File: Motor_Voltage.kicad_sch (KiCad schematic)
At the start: 15 parts

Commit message: mini review notes
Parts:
- gave numbers to parts that had none: 15
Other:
- note added: "V+ and V- not descriptive bruh"
- note added: "V_IN_2 change to output"
- note added: "V_IN_2 to V_IN_MOT to be more descriptive"
- note added: "change HVGND and LVGND global labels into just a hierarchal pin"
- note added: "hierarchal pin works like label"
- note added: "line with line tool and "e""

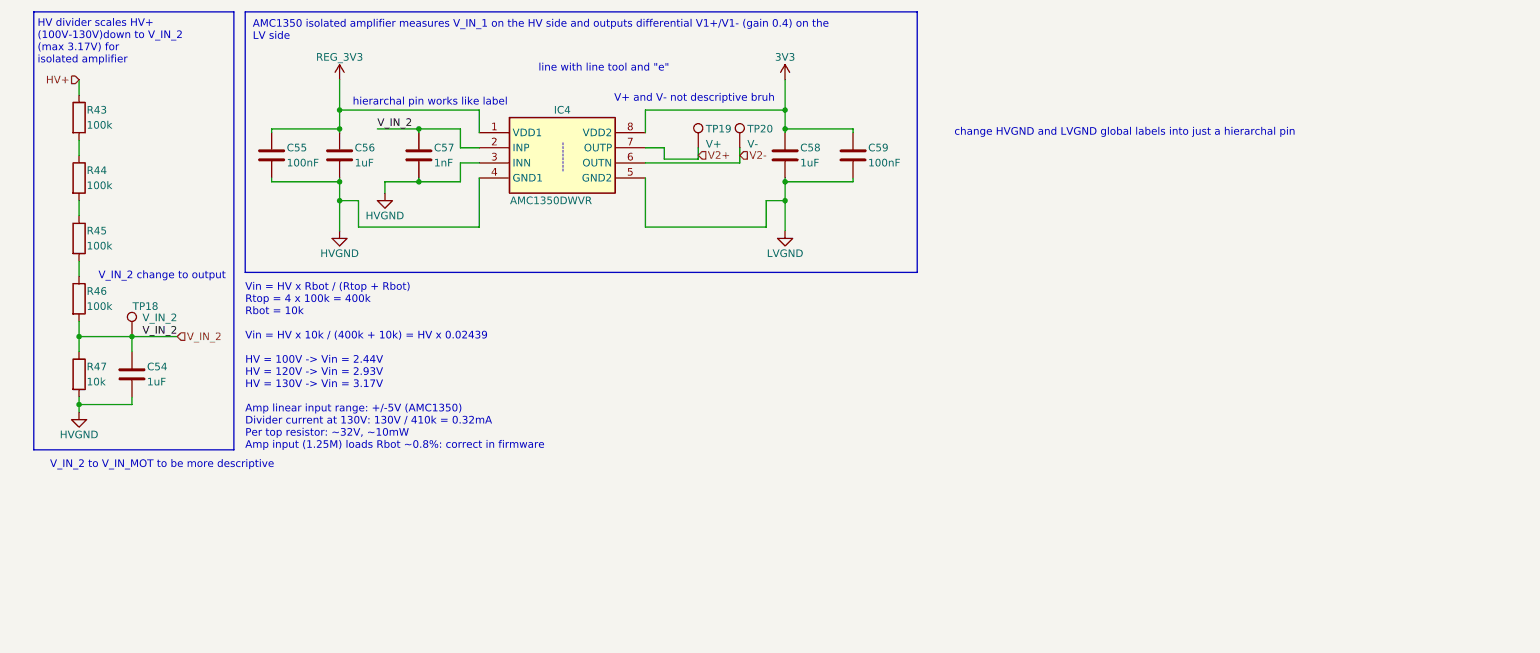
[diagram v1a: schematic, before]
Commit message: fixed battery voltage & motor voltage
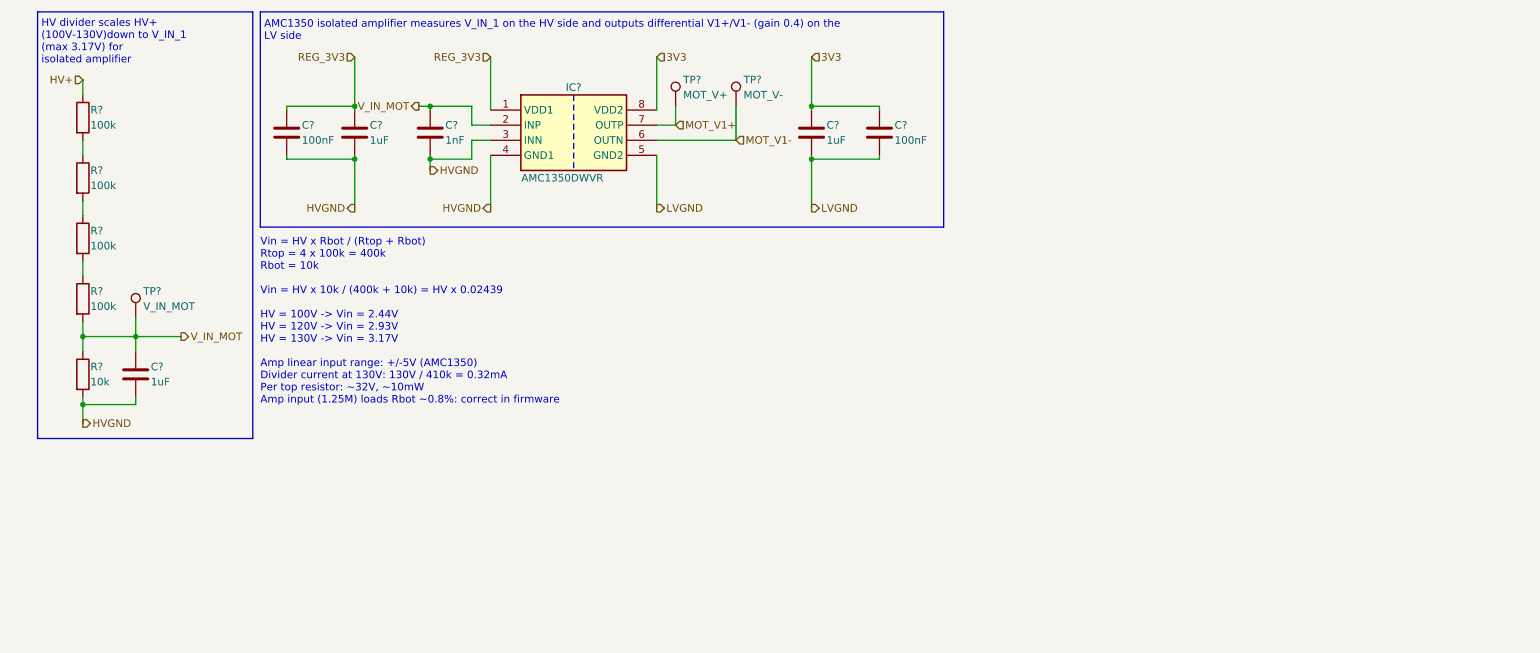
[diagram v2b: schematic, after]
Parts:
- removed C54, C56, C58: 1uF, symbol Device:C
- removed C55, C59: 100nF, symbol Device:C
- removed C57: 1nF, symbol Device:C
- removed IC4: AMC1350DWVR, ActivePrecharge-RevB:SOIC127P1150X280-8N, symbol AMC1350:AMC1350DWVR
- removed R43, R44, R45, R46: 100k, Package_DIP:DIP-8_W7.62mm, symbol Device:R
- removed R47: 10k, Package_DIP:DIP-8_W7.62mm, symbol Device:R
- removed TP18: V_IN_2, symbol Connector:TestPoint
- removed TP19: V+, symbol Connector:TestPoint
- removed TP20: V-, symbol Connector:TestPoint
- added C? (x3): 1uF, symbol Device:C
- added C?: 1nF, symbol Device:C
- added C? (x2): 100nF, symbol Device:C
- added IC?: AMC1350DWVR, ActivePrecharge-RevB:SOIC127P1150X280-8N, symbol AMC1350:AMC1350DWVR
- added R?: 10k, Package_DIP:DIP-8_W7.62mm, symbol Device:R
- added R? (x4): 100k, Package_DIP:DIP-8_W7.62mm, symbol Device:R
- added TP?: V_IN_MOT, TestPoint:TestPoint_Loop_D1.80mm_Drill1.0mm_Beaded, symbol lhrs_misc:Multimeter_TP
- added TP?: MOT_V-, TestPoint:TestPoint_Loop_D1.80mm_Drill1.0mm_Beaded, symbol lhrs_misc:Multimeter_TP
- added TP?: MOT_V+, TestPoint:TestPoint_Loop_D1.80mm_Drill1.0mm_Beaded, symbol lhrs_misc:Multimeter_TP
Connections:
- net 3V3: now also C?.1, C?.1, IC?.8 (VDD2)
- net HV+: now also R?.1
- net HVGND: now also C?.2, C?.2, C?.2, C?.2, IC?.3 (INN), IC?.4 (GND1), R?.2
- net LVGND: now also C?.2, C?.2, IC?.5 (GND2)
- net REG_3V3: now also C?.1, C?.1, IC?.1 (VDD1)
- new net: R?.1, R?.2 (x3)
- new net MOT_V1+: IC?.7 (OUTP), TP?.1
- new net MOT_V1-: IC?.6 (OUTN), TP?.1
- new net V_IN_MOT: C?.1, C?.1, IC?.2 (INP), R?.1, R?.2, TP?.1
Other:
- note added: "HV divider scales HV+ (100V-130V)down to V_IN_1 (max 3.17V) for isolated amplifier"
- note removed: "--------"
- note removed: "HV divider scales HV+ (100V-130V)down to V_IN_2 (max 3.17V) for isolated amplifier"
- note removed: "V+ and V- not descriptive bruh"
- note removed: "V_IN_2 change to output"
- note removed: "V_IN_2 to V_IN_MOT to be more descriptive"
- note removed: "change HVGND and LVGND global labels into just a hierarchal pin"
- note removed: "hierarchal pin works like label"
- note removed: "line with line tool and "e""

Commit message: fixed lv
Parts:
- gave numbers to parts that had none: 15
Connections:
- net MOT_V1+ renamed MOT_V+
- net MOT_V1- renamed MOT_V-
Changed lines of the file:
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@@
 		)
 	)
-	(hierarchical_label "MOT_V1-"
+	(hierarchical_label "MOT_V-"
 		(shape input)
 		(at 132.08 35.56 0)
@@
 		)
 	)
-	(hierarchical_label "MOT_V1+"
+	(hierarchical_label "MOT_V+"
 		(shape input)
 		(at 121.92 33.02 0)
@@
 		(in_pos_files yes)
 		(dnp no)
-		(property "Reference" "TP?"
+		(property "Reference" "TP18"
 			(at 32.385 60.96 0)
 			(show_name no)
@@
 			(project "PS-PrechargeBoard"
 				(path "/74d17fe6-68d4-4bd7-954a-e2bbb58b1f1e/ad0f3840-ec25-4ea7-b025-1d3129a06533/c3a8be03-ea6f-409a-9c75-c47de7f52741"
-					(reference "TP?")
+					(reference "TP18")
 					(unit 1)
 				)
@@
 		(in_pos_files yes)
 		(dnp no)
-		(property "Reference" "C?"
+		(property "Reference" "C56"
 			(at 70.485 33.02 0)
 			(show_name no)
@@
 			(project "PS-PrechargeBoard"
 				(path "/74d17fe6-68d4-4bd7-954a-e2bbb58b1f1e/ad0f3840-ec25-4ea7-b025-1d3129a06533/c3a8be03-ea6f-409a-9c75-c47de7f52741"
-					(reference "C?")
+					(reference "C56")
 					(unit 1)
 				)
@@
 		(in_pos_files yes)
 		(dnp no)
-		(property "Reference" "TP?"
+		(property "Reference" "TP20"
 			(at 133.35 25.4 0)
 			(show_name no)
@@
 			(project "PS-PrechargeBoard"
 				(path "/74d17fe6-68d4-4bd7-954a-e2bbb58b1f1e/ad0f3840-ec25-4ea7-b025-1d3129a06533/c3a8be03-ea6f-409a-9c75-c47de7f52741"
-					(reference "TP?")
+					(reference "TP20")
 					(unit 1)
 				)
@@
 		(in_pos_files yes)
 		(dnp no)
-		(property "Reference" "R?"
+		(property "Reference" "R47"
 			(at 23.495 73.66 0)
 			(show_name no)
@@
 			(project "PS-PrechargeBoard"
 				(path "/74d17fe6-68d4-4bd7-954a-e2bbb58b1f1e/ad0f3840-ec25-4ea7-b025-1d3129a06533/c3a8be03-ea6f-409a-9c75-c47de7f52741"
-					(reference "R?")
+					(reference "R47")
 					(unit 1)
 				)
@@
 		(in_pos_files yes)
 		(dnp no)
-		(property "Reference" "C?"
+		(property "Reference" "C57"
 			(at 83.185 33.02 0)
 			(show_name no)
@@
 			(project "PS-PrechargeBoard"
 				(path "/74d17fe6-68d4-4bd7-954a-e2bbb58b1f1e/ad0f3840-ec25-4ea7-b025-1d3129a06533/c3a8be03-ea6f-409a-9c75-c47de7f52741"
-					(reference "C?")
+					(reference "C57")
 					(unit 1)
 				)
@@
 		(in_pos_files yes)
 		(dnp no)
-		(property "Reference" "C?"
+		(property "Reference" "C54"
 			(at 33.655 73.66 0)
 			(show_name no)
@@
 			(project "PS-PrechargeBoard"
 				(path "/74d17fe6-68d4-4bd7-954a-e2bbb58b1f1e/ad0f3840-ec25-4ea7-b025-1d3129a06533/c3a8be03-ea6f-409a-9c75-c47de7f52741"
-					(reference "C?")
+					(reference "C54")
 					(unit 1)
 				)
@@
 		(in_pos_files yes)
 		(dnp no)
-		(property "Reference" "TP?"
+		(property "Reference" "TP19"
 			(at 123.19 25.4 0)
 			(show_name no)
@@
 			(project "PS-PrechargeBoard"
 				(path "/74d17fe6-68d4-4bd7-954a-e2bbb58b1f1e/ad0f3840-ec25-4ea7-b025-1d3129a06533/c3a8be03-ea6f-409a-9c75-c47de7f52741"
-					(reference "TP?")
+					(reference "TP19")
 					(unit 1)
 				)
@@
 		(in_pos_files yes)
 		(dnp no)
-		(property "Reference" "C?"
+		(property "Reference" "C58"
 			(at 147.32 33.02 0)
 			(show_name no)
@@
 			(project "PS-PrechargeBoard"
 				(path "/74d17fe6-68d4-4bd7-954a-e2bbb58b1f1e/ad0f3840-ec25-4ea7-b025-1d3129a06533/c3a8be03-ea6f-409a-9c75-c47de7f52741"
-					(reference "C?")
+					(reference "C58")
 					(unit 1)
 				)
@@
 		(in_pos_files yes)
 		(dnp no)
-		(property "Reference" "IC?"
+		(property "Reference" "IC4"
 			(at 104.775 26.67 0)
 			(show_name no)
@@
 			(project "PS-PrechargeBoard"
 				(path "/74d17fe6-68d4-4bd7-954a-e2bbb58b1f1e/ad0f3840-ec25-4ea7-b025-1d3129a06533/c3a8be03-ea6f-409a-9c75-c47de7f52741"
-					(reference "IC?")
+					(reference "IC4")
 					(unit 1)
 				)
@@
 		(in_pos_files yes)
 		(dnp no)
-		(property "Reference" "C?"
+		(property "Reference" "C59"
 			(at 158.75 33.02 0)
 			(show_name no)
@@
 			(project "PS-PrechargeBoard"
 				(path "/74d17fe6-68d4-4bd7-954a-e2bbb58b1f1e/ad0f3840-ec25-4ea7-b025-1d3129a06533/c3a8be03-ea6f-409a-9c75-c47de7f52741"
-					(reference "C?")
+					(reference "C59")
 					(unit 1)
 				)
@@
 		(in_pos_files yes)
 		(dnp no)
-		(property "Reference" "R?"
+		(property "Reference" "R43"
 			(at 23.495 30.48 0)
 			(show_name no)
@@
 			(project "PS-PrechargeBoard"
 				(path "/74d17fe6-68d4-4bd7-954a-e2bbb58b1f1e/ad0f3840-ec25-4ea7-b025-1d3129a06533/c3a8be03-ea6f-409a-9c75-c47de7f52741"
-					(reference "R?")
+					(reference "R43")
 					(unit 1)
 				)
@@
 		(in_pos_files yes)
 		(dnp no)
-		(property "Reference" "R?"
+		(property "Reference" "R45"
 			(at 23.495 50.8 0)
 			(show_name no)
@@
 			(project "PS-PrechargeBoard"
 				(path "/74d17fe6-68d4-4bd7-954a-e2bbb58b1f1e/ad0f3840-ec25-4ea7-b025-1d3129a06533/c3a8be03-ea6f-409a-9c75-c47de7f52741"
-					(reference "R?")
+					(reference "R45")
 					(unit 1)
 				)
@@
 		(in_pos_files yes)
 		(dnp no)
-		(property "Reference" "R?"
+		(property "Reference" "R46"
 			(at 23.495 60.96 0)
 			(show_name no)
@@
 			(project "PS-PrechargeBoard"
 				(path "/74d17fe6-68d4-4bd7-954a-e2bbb58b1f1e/ad0f3840-ec25-4ea7-b025-1d3129a06533/c3a8be03-ea6f-409a-9c75-c47de7f52741"
-					(reference "R?")
+					(reference "R46")
 					(unit 1)
 				)
@@
 		(in_pos_files yes)
 		(dnp no)
-		(property "Reference" "C?"
+		(property "Reference" "C55"
 			(at 59.055 33.02 0)
 			(show_name no)
@@
 			(project "PS-PrechargeBoard"
 				(path "/74d17fe6-68d4-4bd7-954a-e2bbb58b1f1e/ad0f3840-ec25-4ea7-b025-1d3129a06533/c3a8be03-ea6f-409a-9c75-c47de7f52741"
-					(reference "C?")
+					(reference "C55")
 					(unit 1)
 				)
@@
 		(in_pos_files yes)
 		(dnp no)
-		(property "Reference" "R?"
+		(property "Reference" "R44"
 			(at 23.495 40.64 0)
 			(show_name no)
@@
 			(project "PS-PrechargeBoard"
 				(path "/74d17fe6-68d4-4bd7-954a-e2bbb58b1f1e/ad0f3840-ec25-4ea7-b025-1d3129a06533/c3a8be03-ea6f-409a-9c75-c47de7f52741"
-					(reference "R?")
-					(unit 1)
-				)
+					(reference "R44")
+					(unit 1)
+				)

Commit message: shifted hierarchical sheets
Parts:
- renumbered C56 to C?, C57 to C?, C54 to C?, C58 to C?, C59 to C?, C55 to C?, IC4 to IC?, R47 to R?, R43 to R?, R45 to R?, R46 to R?, R44 to R?, TP18 to TP?, TP20 to TP?, TP19 to TP?
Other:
- moved on the sheet: C?, IC?, TP?

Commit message: unboxed items to be fixed later
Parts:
- added C6: 10nF, symbol Device:C
- added C?: 1uF, Capacitor_SMD:C_0603_1608Metric_Pad1.08x0.95mm_HandSolder, symbol Device:C
- added R10, R9: 10k, Package_DIP:DIP-8_W7.62mm, symbol Device:R
- added R11, R12: 10k, symbol Device:R
- added R13: 10, symbol Device:R
- added TP?: V_OUT_MOT, TestPoint:TestPoint_Loop_D1.80mm_Drill1.0mm_Beaded, symbol lhrs_misc:Multimeter_TP
- added U3, U?: TLV9002QDRQ1, Package_SO:SOIC-8_3.9x4.9mm_P1.27mm, symbol UTSVT-Misc:TLV9002QDRQ1
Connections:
- net 3V3: now also C?.1, U?.8 (V+)
- net LVGND: now also C6.2, C?.2, R10.2, U?.4 (V-)
- net MOT_V+: now also R9.1
- net MOT_V-: now also R11.1
- new net: R10.1, R9.2, U3.3 (+)
- new net: R11.2, R12.1, U3.2 (-)
- new net: R12.2, R13.1, U3.1
- new net V_OUT_MOT: C6.1, R13.2, TP?.1
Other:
- note added: "Op-amps acting as a unity gain amplifier"

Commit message: added DE1a-12V precharge relay
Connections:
- net LVGND: no longer C6.2, C?.2, C?.2, C?.2, IC?.5 (GND2), U?.4 (V-)
- new net GND: C6.2, C?.2, C?.2, C?.2, IC?.5 (GND2), U?.4 (V-)
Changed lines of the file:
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@@
 		)
 	)
-	(hierarchical_label "LVGND"
-		(shape bidirectional)
+	(hierarchical_label "GND"
+		(shape input)
 		(at 113.03 46.99 0)
 		(effects
@@
 	)
 	(hierarchical_label "HVGND"
-		(shape bidirectional)
+		(shape input)
 		(at 62.23 46.99 180)
 		(effects
@@
 		)
 	)
-	(hierarchical_label "LVGND"
+	(hierarchical_label "GND"
 		(shape bidirectional)
 		(at 139.065 46.99 0)
@@
 	)
 	(hierarchical_label "HVGND"
-		(shape bidirectional)
+		(shape input)
 		(at 85.09 46.99 180)
 		(effects
@@
 	)
 	(hierarchical_label "HVGND"
-		(shape bidirectional)
+		(shape input)
 		(at 74.93 40.64 0)
 		(effects
@@
 	)
 	(hierarchical_label "HVGND"
-		(shape bidirectional)
+		(shape input)
 		(at 22.225 83.185 0)
 		(effects
@@
 			)
 		)
-		(property "Value" "LVGND"
+		(property "Value" "GND"
 			(at 206.375 109.22 0)
 			(show_name no)
@@
 			)
 		)
-		(property "Value" "LVGND"
+		(property "Value" "GND"
 			(at 182.88 113.665 0)
 			(show_name no)

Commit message: V_OUT_BAT & V_OUT_MOT & PRECHARGE_CTRL to MCU
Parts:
- removed C6: 10nF, symbol Device:C
- removed C?: 1uF, Capacitor_SMD:C_0603_1608Metric_Pad1.08x0.95mm_HandSolder, symbol Device:C
- removed R10, R9: 10k, Package_DIP:DIP-8_W7.62mm, symbol Device:R
- removed R11, R12: 10k, symbol Device:R
- removed R13: 10, symbol Device:R
- removed TP?: V_OUT_MOT, TestPoint:TestPoint_Loop_D1.80mm_Drill1.0mm_Beaded, symbol lhrs_misc:Multimeter_TP
- removed U3, U?: TLV9002QDRQ1, Package_SO:SOIC-8_3.9x4.9mm_P1.27mm, symbol UTSVT-Misc:TLV9002QDRQ1
- added C?: 10nF, symbol Device:C
- added C?: 1uF, Capacitor_SMD:C_0603_1608Metric_Pad1.08x0.95mm_HandSolder, symbol Device:C
- added R? (x2): 10k, symbol Device:R
- added R? (x2): 10k, Package_DIP:DIP-8_W7.62mm, symbol Device:R
- added R?: 10, symbol Device:R
- added TP?: V_OUT_MOT, TestPoint:TestPoint_Loop_D1.80mm_Drill1.0mm_Beaded, symbol lhrs_misc:Multimeter_TP
- added U? (x2): TLV9002QDRQ1, Package_SO:SOIC-8_3.9x4.9mm_P1.27mm, symbol UTSVT-Misc:TLV9002QDRQ1
- gave numbers to parts that had none: 15
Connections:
- net GND: now also C?.2, C?.2, R?.2, U?.4 (V-)
- net MOT_V+: now also R?.1
- net MOT_V-: now also R?.1
- net V_OUT_MOT: now also C?.1, R?.2, TP?.1
- net 3V3 renamed 3V3A
- net 3V3A: now also C?.1, U?.8 (V+)
- net REG_3V3 renamed ISO_3V3
- new net: R?.1, R?.2, U?.2 (-)
- new net: R?.1, R?.2, U?.1
- new net: R?.1, R?.2, U?.3 (+)
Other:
- note added: "Op-amp difference stage : MOT_V+ minus MOT_V−, filtered smooth V_OUT_MOT before the ADC"
- note added: "Op-amp power: TLV9002 supply on 3V3A with decoupling"
- note removed: "Op-amps acting as a unity gain amplifier"
